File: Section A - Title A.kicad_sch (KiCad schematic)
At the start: 0 parts

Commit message: First draft of schematic
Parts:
- added C1: 2.2uF, Capacitor_SMD:C_0805_2012Metric, symbol Device:C
- added C10, C2, C9: 0.1uF, Capacitor_SMD:C_0603_1608Metric, symbol Device:C
- added C11, C12, C13, C14, C15, C16, C17, C18, C3, C4: 10uF, Capacitor_SMD:C_1206_3216Metric, symbol Device:C
- added C5, C7: 47nF, Capacitor_SMD:C_0402_1005Metric, symbol Device:C
- added C6: 4.7uF, Capacitor_SMD:C_0603_1608Metric, symbol Device:C
- added C8: 1nF, Capacitor_SMD:C_0402_1005Metric, symbol Device:C
- added D1: LED, symbol Device:LED
- added J1: CE, Connector_PinHeader_2.54mm:PinHeader_1x02_P2.54mm_Vertical, symbol Connector:Conn_01x02_Pin
- added L1: 1uH, Inductor_SMD:L_Bourns_SRP7028A_7.3x6.6mm, symbol Device:L
- added R1: 2R-1W, Resistor_SMD:R_2010_5025Metric, symbol Device:R
- added R2: 4.7kR, Resistor_SMD:R_0402_1005Metric, symbol Device:R
- added R3: 5.24kR, Resistor_SMD:R_0402_1005Metric, symbol Device:R
- added R4: 30.31kR, Resistor_SMD:R_0402_1005Metric, symbol Device:R
- added R5: 6.04kR, Resistor_SMD:R_0402_1005Metric, symbol Device:R
- added R6: 100R, Resistor_SMD:R_0402_1005Metric, symbol Device:R
- added R7: 127kR, Resistor_SMD:R_0402_1005Metric, symbol Device:R
- added R8: 100kR, Resistor_SMD:R_0402_1005Metric, symbol Device:R
- added TP1: QON, Connector_PinHeader_2.54mm:PinHeader_1x01_P2.54mm_Vertical, symbol Connector:TestPoint
- added TP2: Thermistor, Connector_PinHeader_2.54mm:PinHeader_1x01_P2.54mm_Vertical, symbol Connector:TestPoint
- added U1: BQ25672RQMR, solar_station:RQM0029A-MFG, symbol solar_station:BQ25672RQMR
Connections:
- new net: J1.1 (Pin_1), U1.13 (CE_N)
- new net: C12.2, C15.2, C17.2, C9.2, U1.29 (PMID)
- new net: D1.1 (K), U1.1 (STAT)
- new net: R7.1, R8.2, U1.17 (ILIM_HIZ)
- new net: R6.1, U1.18 (BATP)
- new net: C7.2, U1.19 (BTST2)
- new net: R5.1, U1.20 (PROG)
- new net: C8.1, U1.24 (SDRV)
- new net: C7.1, L1.2, U1.26 (SW2)
- new net: C5.2, L1.1, U1.28 (SW1)
- new net: C5.1, U1.4 (BTST1)
- new net: C1.1, R1.2
- new net: D1.2 (A), R2.2
- new net +12V: C2.2, C3.2, C4.2, R1.1, U1.2 (VBUS), U1.3 (VBUS), U1.8 (VAC2), U1.9 (VAC1)
- new net BATTERY_PACK: C11.2, C14.2, R6.2, U1.22 (BAT), U1.23 (BAT)
- new net GND: C1.2, C10.1, C11.1, C12.1, C13.1, C14.1, C15.1, C16.1, C17.1, C18.1, C2.1, C3.1, C4.1, C6.1, C8.2, C9.1, J1.2 (Pin_2), R4.1, R5.2, R8.1, U1.10 (ACDRV2), U1.11 (ACDRV1), U1.27 (GND)
- new net INT_N: U1.21 (INT_N)
- new net QON: TP1.1, U1.12 (QON_N)
- new net REGN: C6.2, R2.1, R3.2, R7.2, U1.5 (REGN)
- new net SCL: U1.14 (SCL)
- new net SDA: U1.15 (SDA)
- new net SYSTEM_LOAD: C10.2, C13.2, C16.2, C18.2, U1.25 (SYS)
- new net THERMISTOR: R3.1, R4.2, TP2.1, U1.16 (TS)
- no-connect marks 0 -> 2
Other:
- title: Sheet Title A -> Solar Charger

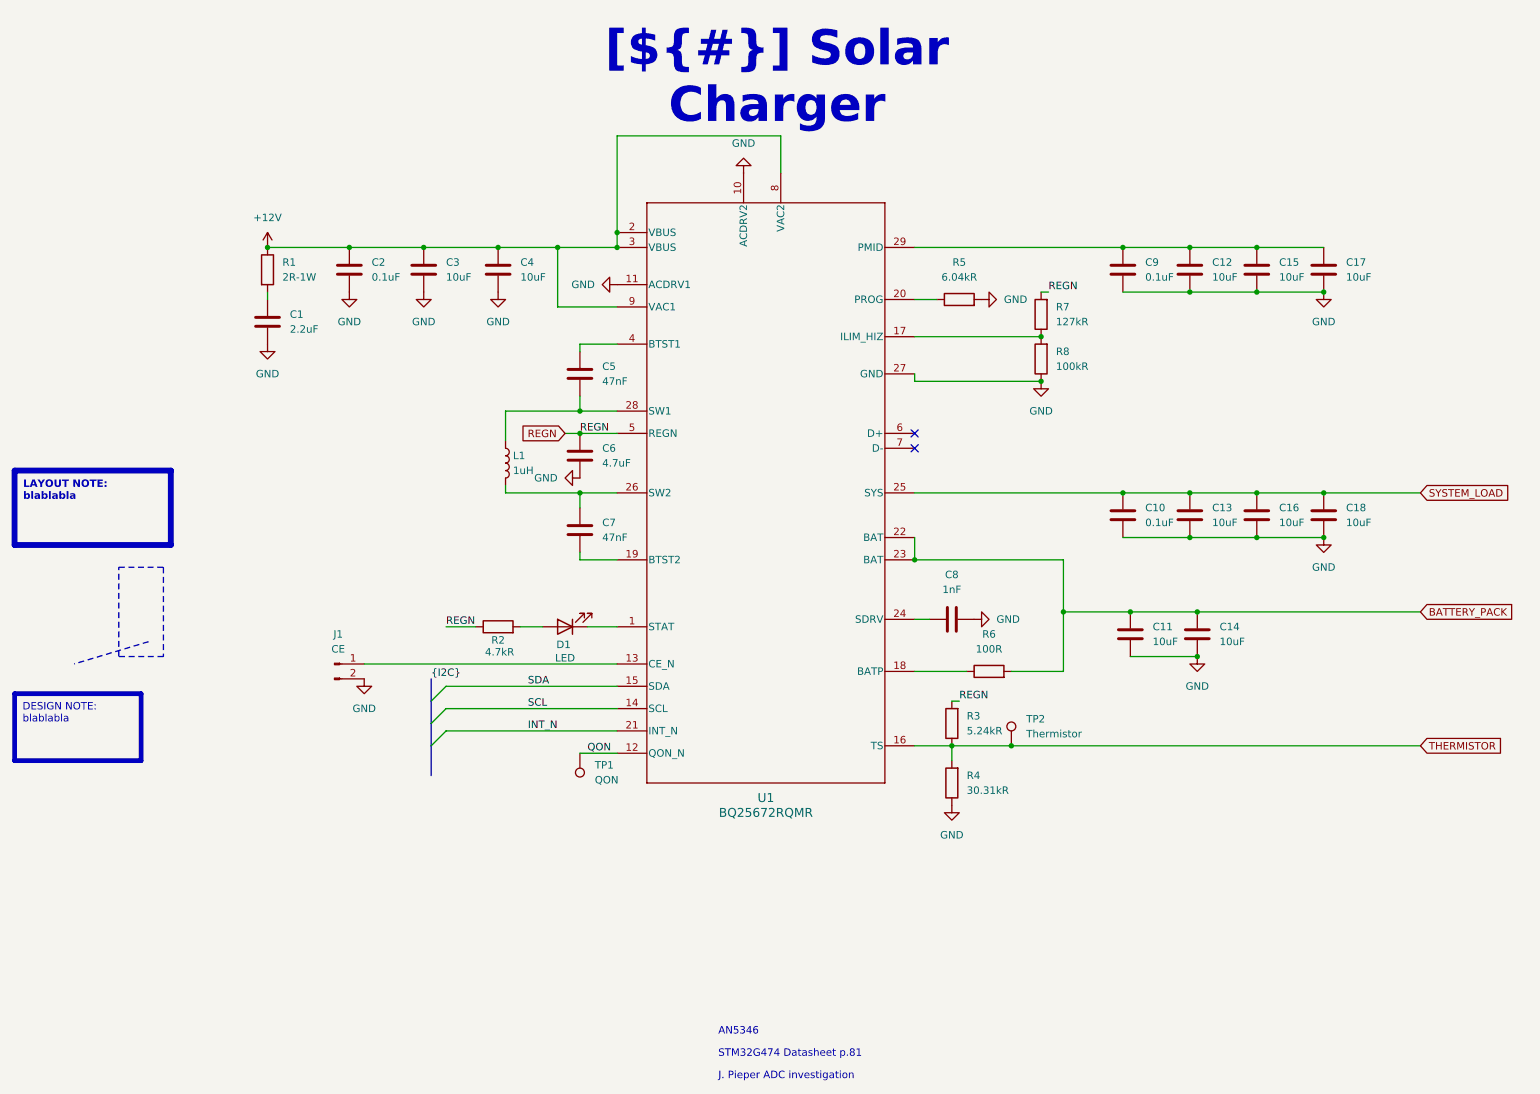
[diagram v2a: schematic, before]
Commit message: Finish schematic
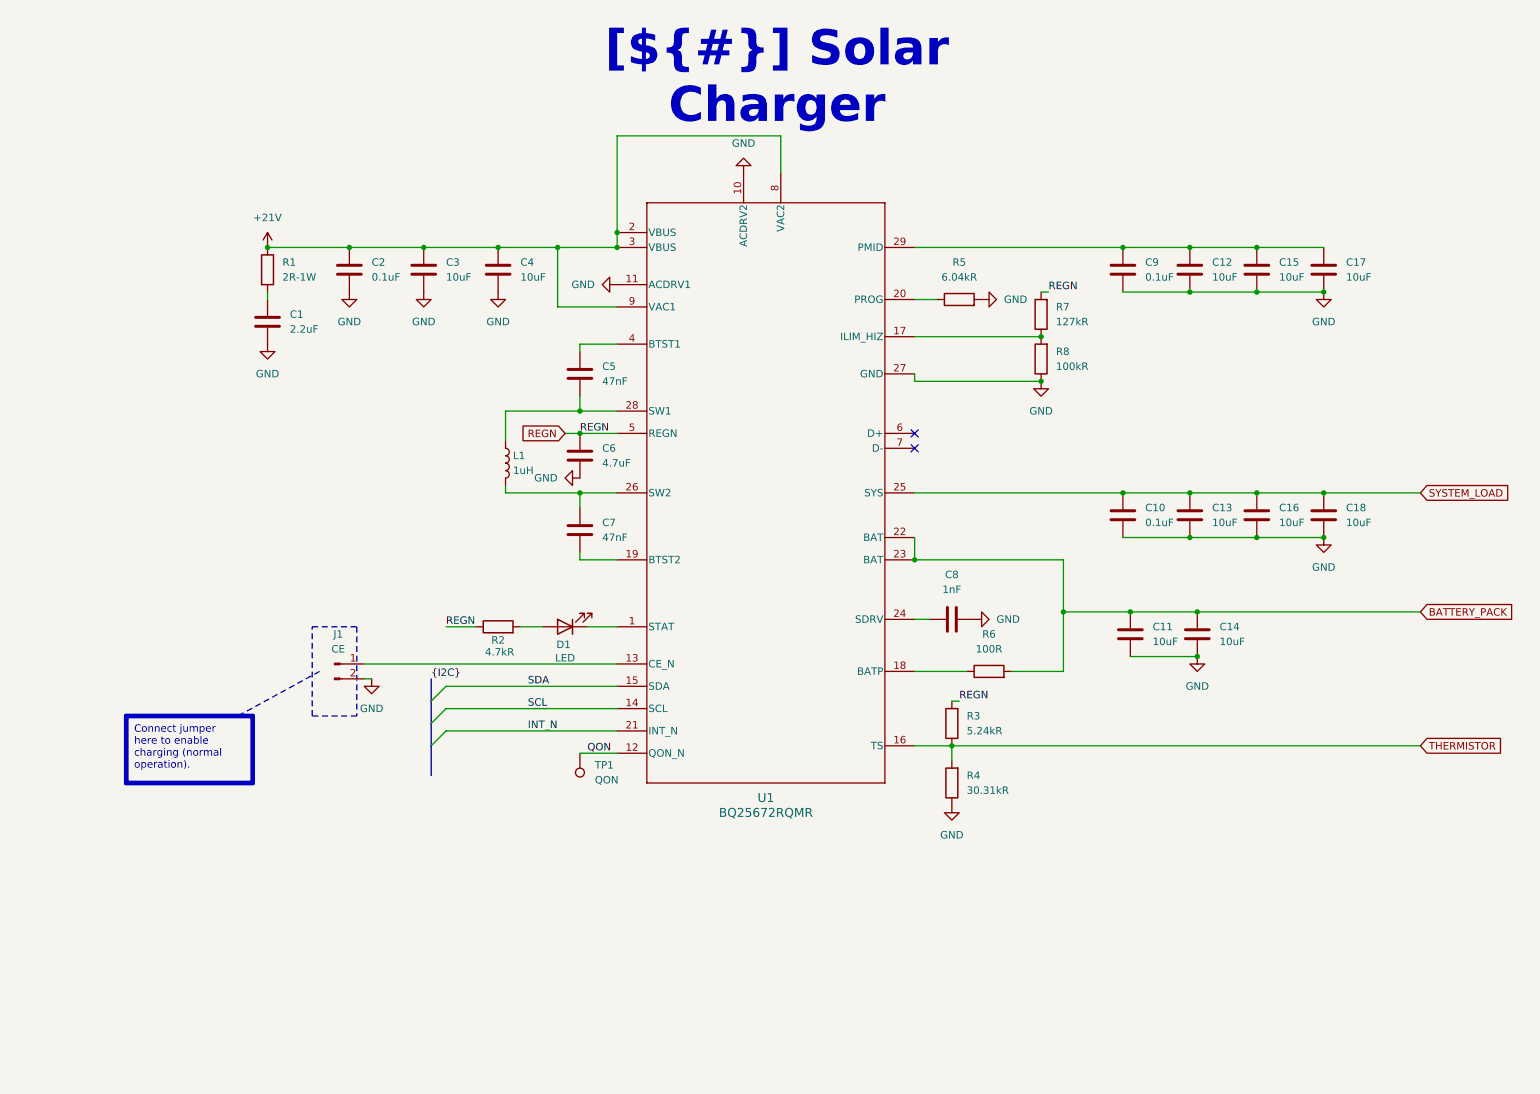
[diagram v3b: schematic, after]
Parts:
- removed TP2: Thermistor, Connector_PinHeader_2.54mm:PinHeader_1x01_P2.54mm_Vertical, symbol Connector:TestPoint
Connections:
- net +12V renamed +21V
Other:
- note removed: "AN5346"
- note removed: "J. Pieper ADC investigation"
- note removed: "STM32G474 Datasheet p.81"
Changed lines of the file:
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@@
 	)
 	(rectangle
-		(start 39.37 105.41)
-		(end 46.99 120.65)
+		(start 72.39 115.57)
+		(end 80.01 130.81)
 		(stroke
 			(width 0)
@@
 		)
 	)
-	(text "J. Pieper ADC investigation"
-		(exclude_from_sim no)
-		(at 141.732 193.04 0)
-		(effects
-			(font
-				(face "Arial")
-				(size 1.27 1.27)
-				(color 0 0 0 1)
-			)
-			(justify left bottom)
-			(href "https://jpieper.com/2023/07/24/stm32g4-adc-performance-part-2/")
-		)
-	)
-	(text "STM32G474 Datasheet p.81"
-		(exclude_from_sim no)
-		(at 141.732 189.23 0)
-		(effects
-			(font
-				(face "Arial")
-				(size 1.27 1.27)
-				(color 0 0 0 1)
-			)
-			(justify left bottom)
-			(href "https://www.st.com/resource/en/datasheet/stm32g474cb.pdf")
-		)
-	)
-	(text "AN5346"
-		(exclude_from_sim no)
-		(at 141.732 185.42 0)
-		(effects
-			(font
-				(face "Arial")
-				(size 1.27 1.27)
-				(color 0 0 0 1)
-			)
-			(justify left bottom)
-			(href "https://www.st.com/resource/en/application_note/an5346-stm32g4-adc-use-tips-and-recommendations-stmicroelectronics.pdf")
-		)
-	)
-	(text_box "LAYOUT NOTE:\nblablabla"
-		(exclude_from_sim no)
-		(at 21.59 88.9 0)
-		(size 26.67 12.7)
-		(margins 1.4525 1.4525 1.4525 1.4525)
-		(stroke
-			(width 1)
-			(type solid)
-			(color 0 0 255 1)
-		)
-		(fill
-			(type none)
-		)
-		(effects
-			(font
-				(face "Arial")
-				(size 1.27 1.27)
-				(thickness 0.4)
-				(bold yes)
-				(color 0 0 255 1)
-			)
-			(justify left top)
-		)
-	)
 	(text_box "[${#}] ${TITLE}"
 		(exclude_from_sim no)
@@
 		)
 	)
-	(text_box "DESIGN NOTE:\nblablabla"
+	(text_box "Connect jumper here to enable charging (normal operation)."
 		(exclude_from_sim no)
-		(at 21.59 127 0)
+		(at 40.64 130.81 0)
 		(size 21.59 11.43)
 		(margins 1.3525 1.3525 1.3525 1.3525)
@@
 	)
 	(junction
-		(at 191.77 135.89)
-		(diameter 0)
-		(color 0 0 0 0)
-	)
-	(junction
 		(at 222.25 50.8)
 		(diameter 0)
@@
 	(wire
 		(pts
-			(xy 181.61 135.89) (xy 191.77 135.89)
+			(xy 181.61 135.89) (xy 261.62 135.89)
 		)
 		(stroke
@@
 	(wire
 		(pts
-			(xy 191.77 135.89) (xy 261.62 135.89)
+			(xy 175.26 114.3) (xy 177.8 114.3)
 		)
 		(stroke
@@
 	(wire
 		(pts
-			(xy 175.26 114.3) (xy 177.8 114.3)
+			(xy 104.14 50.8) (xy 114.3 50.8)
 		)
 		(stroke
@@
 	(wire
 		(pts
-			(xy 104.14 50.8) (xy 114.3 50.8)
+			(xy 175.26 73.66) (xy 196.85 73.66)
 		)
 		(stroke
@@
 	(wire
 		(pts
-			(xy 175.26 73.66) (xy 196.85 73.66)
+			(xy 114.3 50.8) (xy 124.46 50.8)
 		)
 		(stroke
@@
 	(wire
 		(pts
-			(xy 114.3 50.8) (xy 124.46 50.8)
+			(xy 82.55 124.46) (xy 81.28 124.46)
 		)
 		(stroke
@@
 	(polyline
 		(pts
-			(xy 44.45 118.11) (xy 31.75 121.92)
+			(xy 73.66 123.19) (xy 59.69 130.81)
 		)
 		(stroke
@@
 	(symbol
 		(lib_id "power:GND")
-		(at 81.28 124.46 0)
+		(at 82.55 124.46 0)
 		(unit 1)
 		(exclude_from_sim no)
@@
 		(fields_autoplaced yes)
 		(property "Reference" "#PWR04"
-			(at 81.28 130.81 0)
+			(at 82.55 130.81 0)
 			(effects
 				(font
@@
 		)
 		(property "Value" "GND"
-			(at 81.28 129.54 0)
+			(at 82.55 129.54 0)
 			(effects
 				(font
@@
 		)
 		(property "Footprint" ""
-			(at 81.28 124.46 0)
+			(at 82.55 124.46 0)
 			(effects
 				(font
@@
 		)
 		(property "Datasheet" ""
-			(at 81.28 124.46 0)
+			(at 82.55 124.46 0)
 			(effects
 				(font
@@
 		)
 		(property "Description" "Power symbol creates a global label with name \"GND\" , ground"
-			(at 81.28 124.46 0)
+			(at 82.55 124.46 0)
 			(effects
 				(font
@@
 			)
 		)
-		(property "Value" "+12V"
+		(property "Value" "+21V"
 			(at 64.77 45.72 0)
 			(effects
@@
 					(unit 1)
 				)
-			)
-		)
-	)
-	(symbol
-		(lib_id "Connector:TestPoint")
-		(at 191.77 135.89 0)
-		(unit 1)
-		(exclude_from_sim no)
-		(in_bom yes)
-		(on_board yes)
-		(dnp no)
-		(fields_autoplaced yes)
-		(property "Reference" "TP2"
-			(at 194.31 131.3179 0)
-			(effects
-				(font
-					(size 1.27 1.27)
-				)
-				(justify left)
-			)
-		)
-		(property "Value" "Thermistor"
-			(at 194.31 133.8579 0)
-			(effects
-				(font
-					(size 1.27 1.27)
-				)
-				(justify left)
-			)
-		)
-		(property "Footprint" "Connector_PinHeader_2.54mm:PinHeader_1x01_P2.54mm_Vertical"
-			(at 196.85 135.89 0)
-			(effects
-				(font
-					(size 1.27 1.27)
-				)
-				(hide yes)
-			)
-		)
-		(property "Datasheet" "~"
-			(at 196.85 135.89 0)
-			(effects
-				(font
-					(size 1.27 1.27)
-				)
-				(hide yes)
-			)
-		)
-		(property "Description" "test point"
-			(at 191.77 135.89 0)
-			(effects
-				(font
-					(size 1.27 1.27)
-				)
-				(hide yes)
-			)
-		)
-		(pin "1"
-		)
-		(instances
-			(project ""
-				(path "/ea8c4f5e-7a49-4faf-a994-dbc85ed86b0a"
-					(reference "TP1")
-					(unit 1)
-				)
-			)
-			(project "solar_smart_station"
-				(path "/f9e05184-c88b-4a88-ae9c-ab2bdb32be7c/c5103ceb-5325-4a84-a025-9638a412984e/f06537ee-772d-44d3-8c50-e0ba41038c9c"
-					(reference "TP2")
-					(unit 1)
-				)

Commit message: First layout
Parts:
- removed J1: CE, Connector_PinHeader_2.54mm:PinHeader_1x02_P2.54mm_Vertical, symbol Connector:Conn_01x02_Pin
- C10, C2, C9: footprint Capacitor_SMD:C_0603_1608Metric -> Capacitor_SMD:C_0402_1005Metric
- D1: footprint (none) -> LED_SMD:LED_0603_1608Metric
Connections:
- net CE_N: now reaches U1.13 (CE_N)
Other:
- moved on the sheet: C17

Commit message: Fix ERC
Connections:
- net REGN renamed REGN_5V
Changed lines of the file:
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@@
 	(wire
 		(pts
-			(xy 115.57 82.55) (xy 118.11 82.55)
+			(xy 100.33 82.55) (xy 118.11 82.55)
 		)
 		(stroke
@@
 	(wire
 		(pts
+			(xy 64.77 48.26) (xy 64.77 50.8)
+		)
+		(stroke
+			(width 0)
+			(type default)
+		)
+	)
+	(wire
+		(pts
 			(xy 223.52 113.03) (xy 261.62 113.03)
 		)
@@
 		(pts
 			(xy 222.25 58.42) (xy 233.68 58.42)
+		)
+		(stroke
+			(width 0)
+			(type default)
+		)
+	)
+	(wire
+		(pts
+			(xy 64.77 68.58) (xy 64.77 67.31)
 		)
 		(stroke
@@
 		)
 	)
-	(global_label "REGN"
+	(global_label "REGN_5V"
 		(shape input)
-		(at 115.57 82.55 180)
+		(at 100.33 82.55 180)
 		(fields_autoplaced yes)
 		(effects
@@
 		)
 		(property "Intersheetrefs" "${INTERSHEET_REFS}"
-			(at 107.5653 82.55 0)
+			(at 89.0596 82.55 0)
 			(effects
 				(font
@@
 	(symbol
 		(lib_id "power:+12V")
-		(at 64.77 50.8 0)
+		(at 64.77 48.26 0)
 		(unit 1)
 		(exclude_from_sim no)
@@
 		(fields_autoplaced yes)
 		(property "Reference" "#PWR01"
-			(at 64.77 54.61 0)
+			(at 64.77 52.07 0)
 			(effects
 				(font
@@
 		)
 		(property "Value" "+21V"
-			(at 64.77 45.72 0)
+			(at 64.77 43.18 0)
 			(effects
 				(font
@@
 		)
 		(property "Footprint" ""
-			(at 64.77 50.8 0)
+			(at 64.77 48.26 0)
 			(effects
 				(font
@@
 		)
 		(property "Datasheet" ""
-			(at 64.77 50.8 0)
+			(at 64.77 48.26 0)
 			(effects
 				(font
@@
 		)
 		(property "Description" "Power symbol creates a global label with name \"+12V\""
-			(at 64.77 50.8 0)
+			(at 64.77 48.26 0)
 			(effects
 				(font
@@
 	(symbol
 		(lib_id "power:GND")
-		(at 64.77 67.31 0)
+		(at 64.77 68.58 0)
 		(unit 1)
 		(exclude_from_sim no)
@@
 		(fields_autoplaced yes)
 		(property "Reference" "#PWR02"
+			(at 64.77 74.93 0)
+			(effects
+				(font
+					(size 1.27 1.27)
+				)
+				(hide yes)
+			)
+		)
+		(property "Value" "GND"
 			(at 64.77 73.66 0)
 			(effects
@@
 					(size 1.27 1.27)
 				)
-				(hide yes)
-			)
-		)
-		(property "Value" "GND"
-			(at 64.77 72.39 0)
-			(effects
-				(font
-					(size 1.27 1.27)
-				)
 			)
 		)
 		(property "Footprint" ""
-			(at 64.77 67.31 0)
+			(at 64.77 68.58 0)
 			(effects
 				(font
@@
 		)
 		(property "Datasheet" ""
-			(at 64.77 67.31 0)
+			(at 64.77 68.58 0)
 			(effects
 				(font
@@
 		)
 		(property "Description" "Power symbol creates a global label with name \"GND\" , ground"
-			(at 64.77 67.31 0)
-			(effects
-				(font
+			(at 64.77 68.58 0)
+			(effects
+				(font
